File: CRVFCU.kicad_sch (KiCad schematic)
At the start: 150 parts, among them J1 TagConnect_TC2030, J3 USB_C_Receptacle_USB2.0_16P, J4 Micro_SD_Card_Det2, Q3 DMG2301L, Q4 BC818, Q5 DMG2301L, Q6 DMG2301L, SW1 SW_Omron_B3FS, SW2 SW_Nidec_CAS-120A1, U1 MS5611-01BA, U10 W25Q128JVS, U11 CM1624, U12 ESDALC6V1W5, U13 USBLC6-2SC6, U14 USBLC6-2SC6, U15 MAX17049, U16 SI7232DN-T1, U17 SN74LV1T34DCK, U2 STM32H747IITx, U3 LIS2MDL, U4 ICM-45686, U5 FXMA108, U6 AP1117-50, U7 AP1117-33, U8 SI7232DN-T1, U9 USBLC6-4SC6, Y1 32.768khz, Y2 Crystal_GND24, Y3 32.768khz

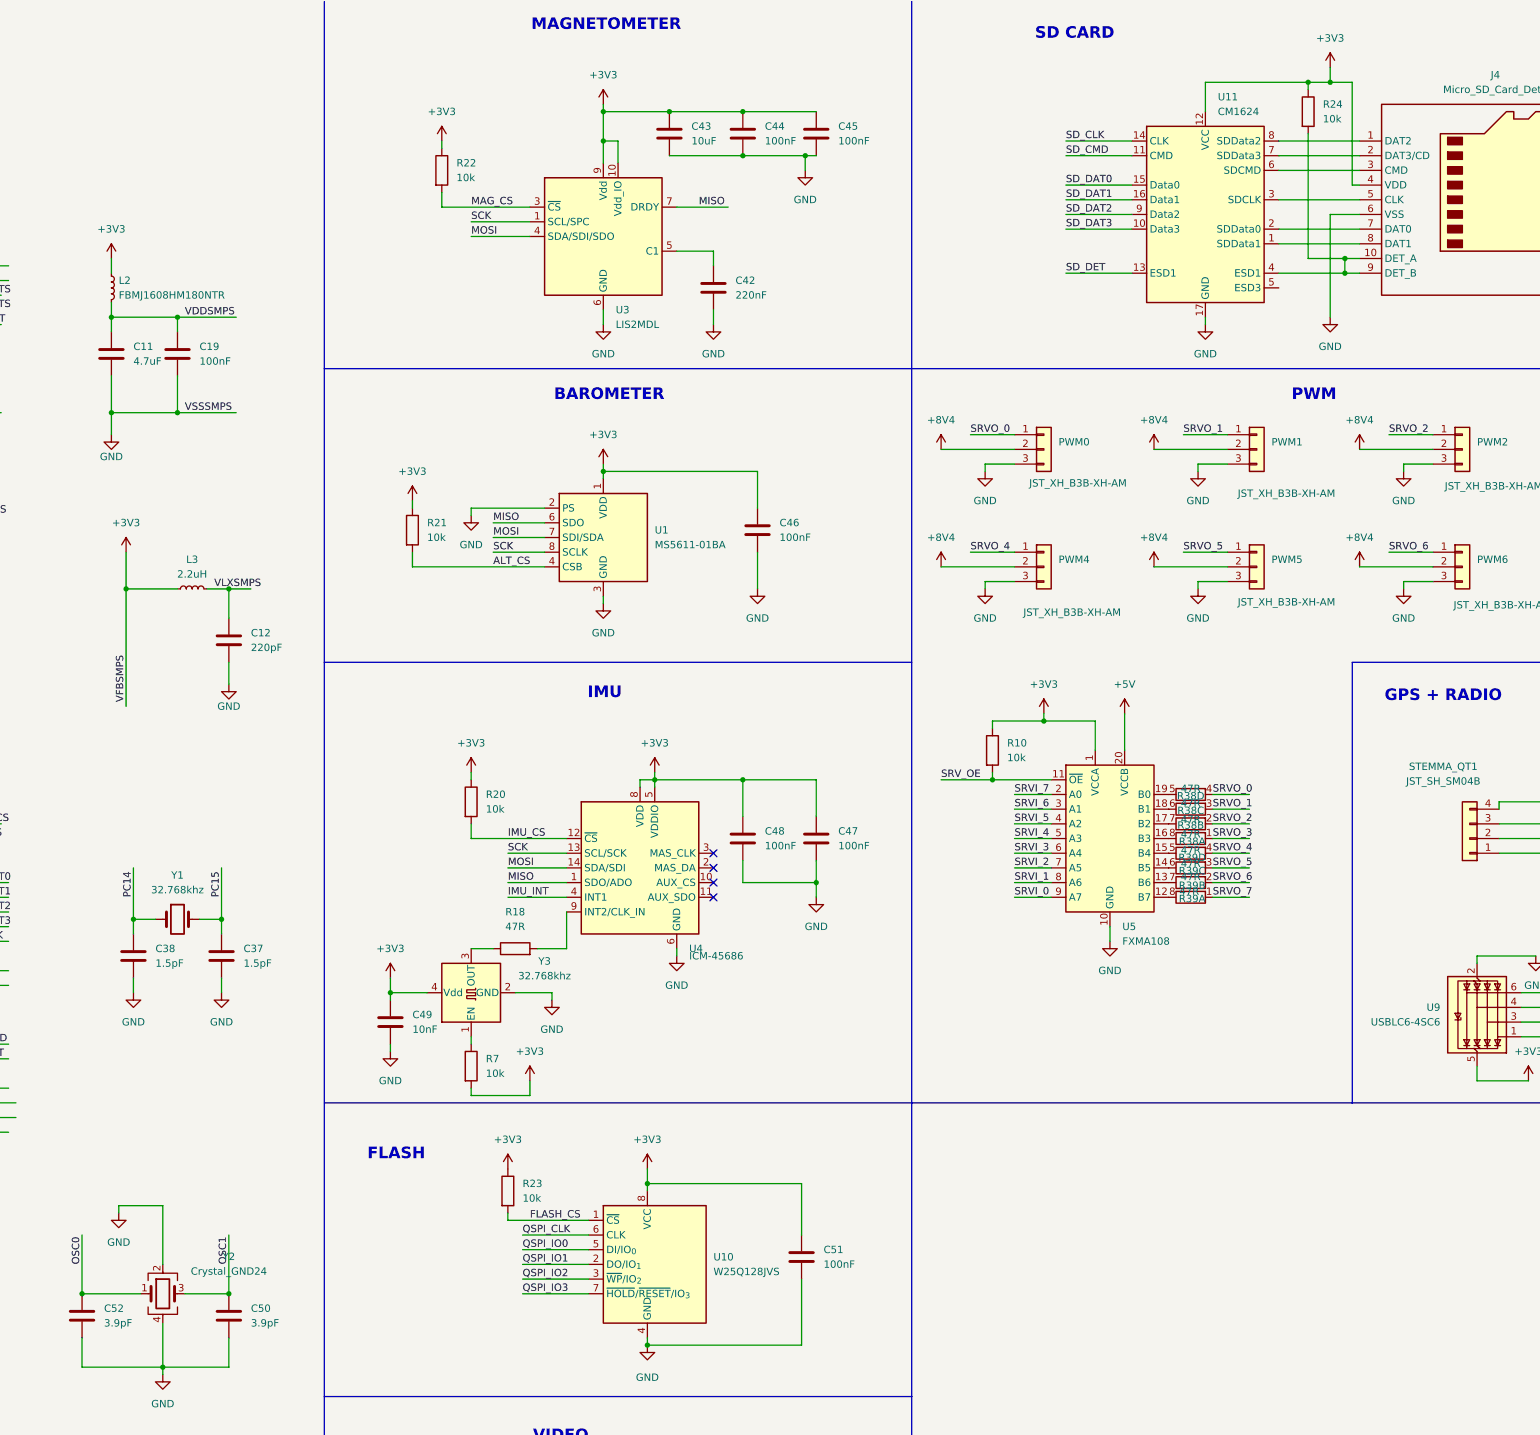
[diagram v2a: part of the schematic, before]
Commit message: rounded corners, added silkscreens, fixed 25mhz oscillator, missing logos but basically finalized
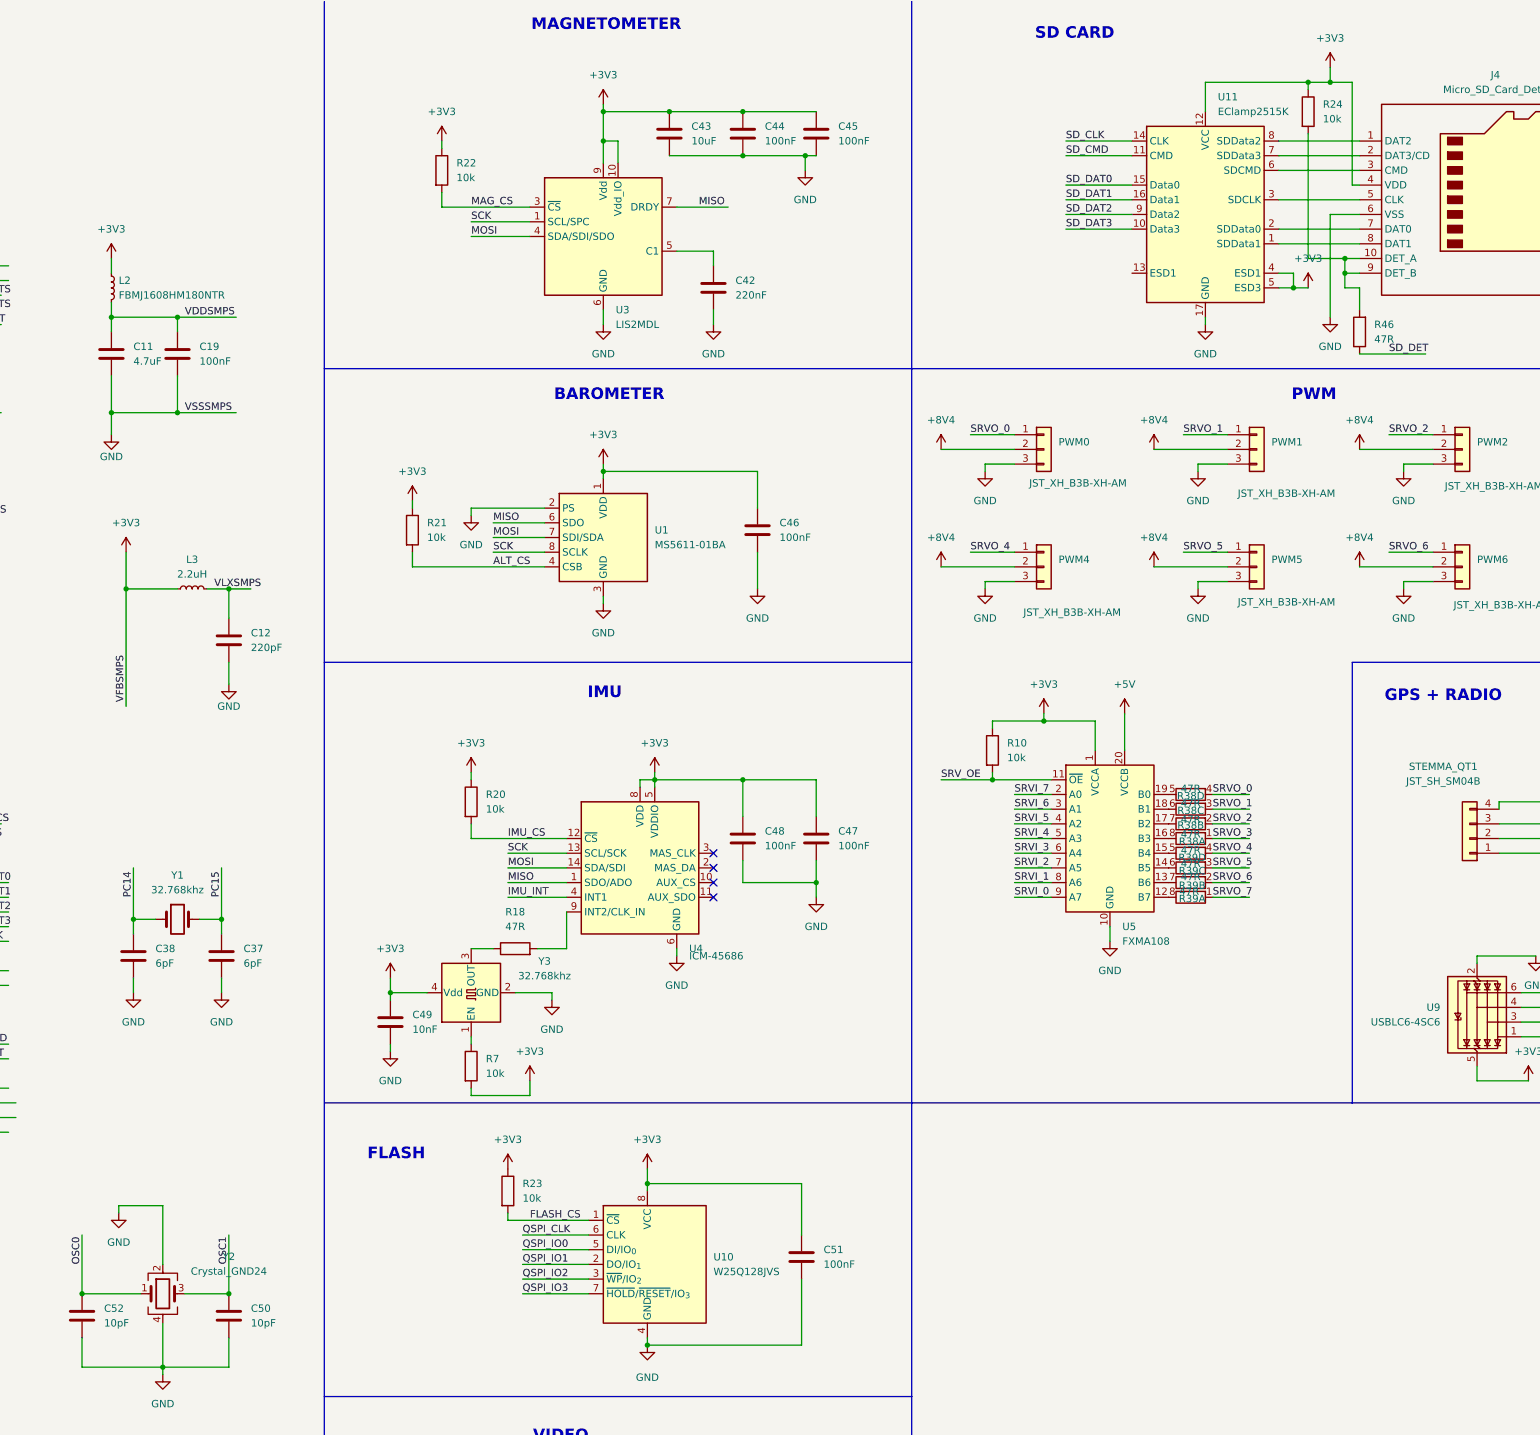
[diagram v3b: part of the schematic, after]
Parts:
- added R46: 47R, Resistor_SMD:R_0402_1005Metric, symbol Device:R
- C37, C38: value 1.5pF -> 6pF
- C50, C52: value 3.9pF -> 10pF
- U11: value CM1624 -> EClamp2515K
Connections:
- net +3V3: now also U11.4 (ESD1), U11.5 (ESD3)
- net SD_DET: now also R46.1; no longer U11.13 (ESD1)
- net at J4.10 (DET_A), J4.9 (DET_B), R24.2: now also R46.2; no longer U11.4 (ESD1)
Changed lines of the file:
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@@
 	)
 	(junction
+		(at 497.84 62.23)
+		(diameter 0)
+		(color 0 0 0 0)
+	)
+	(junction
 		(at 184.15 295.91)
 		(diameter 0)
@@
 	)
 	(junction
-		(at 506.73 59.69)
-		(diameter 0)
-		(color 0 0 0 0)
-	)
-	(junction
 		(at 293.37 67.31)
 		(diameter 0)
@@
 	)
 	(junction
+		(at 506.73 59.69)
+		(diameter 0)
+		(color 0 0 0 0)
+	)
+	(junction
 		(at 162.56 241.3)
 		(diameter 0)
@@
 	(wire
 		(pts
+			(xy 509.27 73.66) (xy 520.7 73.66)
+		)
+		(stroke
+			(width 0)
+			(type default)
+		)
+	)
+	(wire
+		(pts
 			(xy 402.59 161.29) (xy 402.59 165.1)
 		)
@@
 	(wire
 		(pts
+			(xy 509.27 62.23) (xy 506.73 62.23)
+		)
+		(stroke
+			(width 0)
+			(type default)
+		)
+	)
+	(wire
+		(pts
 			(xy 27.94 36.83) (xy 27.94 38.1)
 		)
@@
 	(wire
 		(pts
+			(xy 509.27 66.04) (xy 509.27 62.23)
+		)
+		(stroke
+			(width 0)
+			(type default)
+		)
+	)
+	(wire
+		(pts
 			(xy 415.29 147.32) (xy 415.29 153.67)
 		)
@@
 	(wire
 		(pts
+			(xy 497.84 59.69) (xy 497.84 62.23)
+		)
+		(stroke
+			(width 0)
+			(type default)
+		)
+	)
+	(wire
+		(pts
 			(xy 196.85 275.59) (xy 209.55 275.59)
 		)
@@
 	(wire
 		(pts
-			(xy 495.3 59.69) (xy 506.73 59.69)
+			(xy 497.84 62.23) (xy 500.38 62.23)
 		)
 		(stroke
@@
 	(wire
 		(pts
+			(xy 495.3 62.23) (xy 497.84 62.23)
+		)
+		(stroke
+			(width 0)
+			(type default)
+		)
+	)
+	(wire
+		(pts
 			(xy 402.59 31.75) (xy 415.29 31.75)
 		)
@@
 	(wire
 		(pts
+			(xy 495.3 59.69) (xy 497.84 59.69)
+		)
+		(stroke
+			(width 0)
+			(type default)
+		)
+	)
+	(wire
+		(pts
 			(xy 48.26 125.73) (xy 48.26 127)
 		)
@@
 	(wire
 		(pts
-			(xy 458.47 59.69) (xy 469.9 59.69)
-		)
-		(stroke
-			(width 0)
-			(type default)
-		)
-	)
-	(wire
-		(pts
 			(xy 222.25 284.48) (xy 222.25 285.75)
 		)
@@
 	(wire
 		(pts
+			(xy 506.73 62.23) (xy 506.73 59.69)
+		)
+		(stroke
+			(width 0)
+			(type default)
+		)
+	)
+	(wire
+		(pts
 			(xy 50.8 341.63) (xy 50.8 342.9)
 		)
@@
 		)
 	)
-	(label "SD_DET"
-		(at 458.47 59.69 0)
-		(effects
-			(font
-				(size 1.27 1.27)
-			)
-			(justify left bottom)
-		)
-	)
 	(label "SRVI_3"
 		(at 264.16 160.02 0)
@@
 		)
 	)
+	(label "SD_DET"
+		(at 514.35 73.66 0)
+		(effects
+			(font
+				(size 1.27 1.27)
+			)
+			(justify left bottom)
+		)
+	)
 	(label "PYO1"
 		(at 293.37 330.2 0)
@@
 	)
 	(symbol
+		(lib_id "power:+3V3")
+		(at 500.38 62.23 0)
+		(unit 1)
+		(exclude_from_sim no)
+		(in_bom yes)
+		(on_board yes)
+		(dnp no)
+		(fields_autoplaced yes)
+		(property "Reference" "#PWR0156"
+			(at 500.38 66.04 0)
+			(effects
+				(font
+					(size 1.27 1.27)
+				)
+				(hide yes)
+			)
+		)
+		(property "Value" "+3V3"
+			(at 500.38 57.15 0)
+			(effects
+				(font
+					(size 1.27 1.27)
+				)
+			)
+		)
+		(property "Footprint" ""
+			(at 500.38 62.23 0)
+			(effects
+				(font
+					(size 1.27 1.27)
+				)
+				(hide yes)
+			)
+		)
+		(property "Datasheet" ""
+			(at 500.38 62.23 0)
+			(effects
+				(font
+					(size 1.27 1.27)
+				)
+				(hide yes)
+			)
+		)
+		(property "Description" "Power symbol creates a global label with name \"+3V3\""
+			(at 500.38 62.23 0)
+			(effects
+				(font
+					(size 1.27 1.27)
+				)
+				(hide yes)
+			)
+		)
+		(pin "1"
+		)
+		(instances
+			(project "CRVFCU"
+				(path "/ad8e65f5-b3fb-4c85-9d9e-17b5feb23144"
+					(reference "#PWR0156")
+					(unit 1)
+				)
+			)
+		)
+	)
+	(symbol
 		(lib_id "power:GND")
 		(at 137.16 82.55 0)
@@
 			)
 		)
-		(property "Value" "1.5pF"
+		(property "Value" "6pF"
 			(at 316.23 179.0699 0)
 			(effects
@@
 			)
 		)
-		(property "Value" "CM1624"
+		(property "Value" "EClamp2515K"
 			(at 484.7433 31.75 0)
 			(effects
@@
 			)
 		)
-		(property "Value" "3.9pF"
+		(property "Value" "10pF"
 			(at 317.5 241.2999 0)
 			(effects
@@
 			)
 		)
-		(property "Value" "1.5pF"
+		(property "Value" "6pF"
 			(at 300.99 179.0699 0)
 			(effects
@@
 	)
 	(symbol
+		(lib_id "Device:R")
+		(at 509.27 69.85 180)
+		(unit 1)
+		(exclude_from_sim no)
+		(in_bom yes)
+		(on_board yes)
+		(dnp no)
+		(fields_autoplaced yes)
+		(property "Reference" "R46"
+			(at 511.81 68.5799 0)
+			(effects
+				(font
+					(size 1.27 1.27)
+				)
+				(justify right)
+			)
+		)
+		(property "Value" "47R"
+			(at 511.81 71.1199 0)
+			(effects
+				(font
+					(size 1.27 1.27)
+				)
+				(justify right)
+			)
+		)
+		(property "Footprint" "Resistor_SMD:R_0402_1005Metric"
+			(at 511.048 69.85 90)
+			(effects
+				(font
+					(size 1.27 1.27)
+				)
+				(hide yes)
+			)
+		)
+		(property "Datasheet" "~"
+			(at 509.27 69.85 0)
+			(effects
+				(font
+					(size 1.27 1.27)
+				)
+				(hide yes)
+			)
+		)
+		(property "Description" "Resistor"
+			(at 509.27 69.85 0)
+			(effects
+				(font
+					(size 1.27 1.27)
+				)
+				(hide yes)
+			)
+		)
+		(pin "1"
+		)
+		(pin "2"
+		)
+		(instances
+			(project "CRVFCU"
+				(path "/ad8e65f5-b3fb-4c85-9d9e-17b5feb23144"
+					(reference "R46")
+					(unit 1)
+				)
+			)
+		)
+	)
+	(symbol
 		(lib_id "Device:C")
 		(at 260.35 280.67 0)
@@
 			)
 		)
-		(property "Value" "3.9pF"
+		(property "Value" "10pF"
 			(at 292.1 241.2999 0)
 			(effects

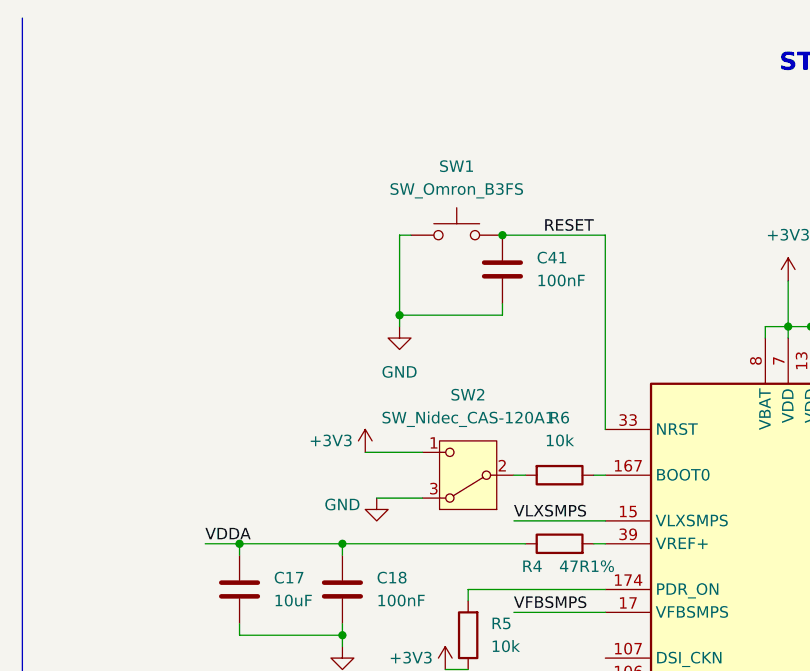
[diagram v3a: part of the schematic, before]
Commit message: changed rst and boot to headers
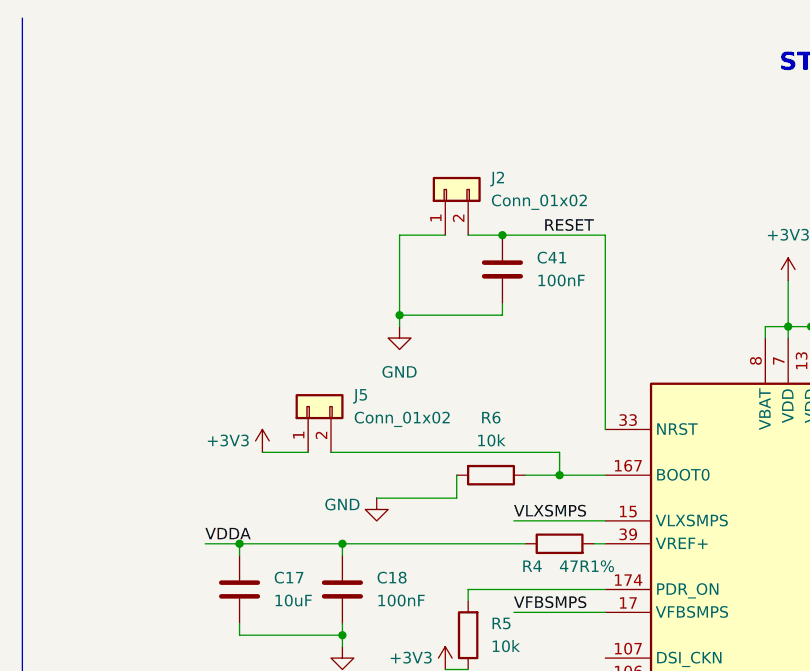
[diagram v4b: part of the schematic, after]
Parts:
- removed SW1: SW_Omron_B3FS, Button_Switch_SMD:SW_SPST_FSMSM, symbol Switch:SW_Omron_B3FS
- removed SW2: SW_Nidec_CAS-120A1, Button_Switch_SMD:Nidec_Copal_CAS-120A, symbol Switch:SW_Nidec_CAS-120A1
- added J2, J5: Conn_01x02, Connector_PinHeader_2.54mm:PinHeader_1x02_P2.54mm_Vertical, symbol Connector_Generic:Conn_01x02
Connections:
- net +3V3: now also J5.1 (Pin_1)
- net GND: now also R6.2, J2.1 (Pin_1)
- net RESET: now also J2.2 (Pin_2)
- net at R6.1, U2.167 (BOOT0): now also J5.2 (Pin_2)
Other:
- moved on the sheet: R6

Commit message: added vref caps and changed some cap values
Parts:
- added C53, C55: 100nF, Capacitor_SMD:C_0402_1005Metric, symbol Device:C
- added C54: 1uF, Capacitor_SMD:C_0402_1005Metric, symbol Device:C
- C17: value 10uF -> 1uF
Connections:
- net +5V: now also C53.1
- net GND: now also J4.10 (DET_A), J4.11 (SHIELD), C53.2, C54.2, C55.2
- net VREF: now reaches R4.2, U2.39 (VREF+)
- net VREF: now also C54.1, C55.1
- net at J4.9 (DET_B), R24.2, R46.2: no longer J4.10 (DET_A)
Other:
- moved on the sheet: C17, C18, R4

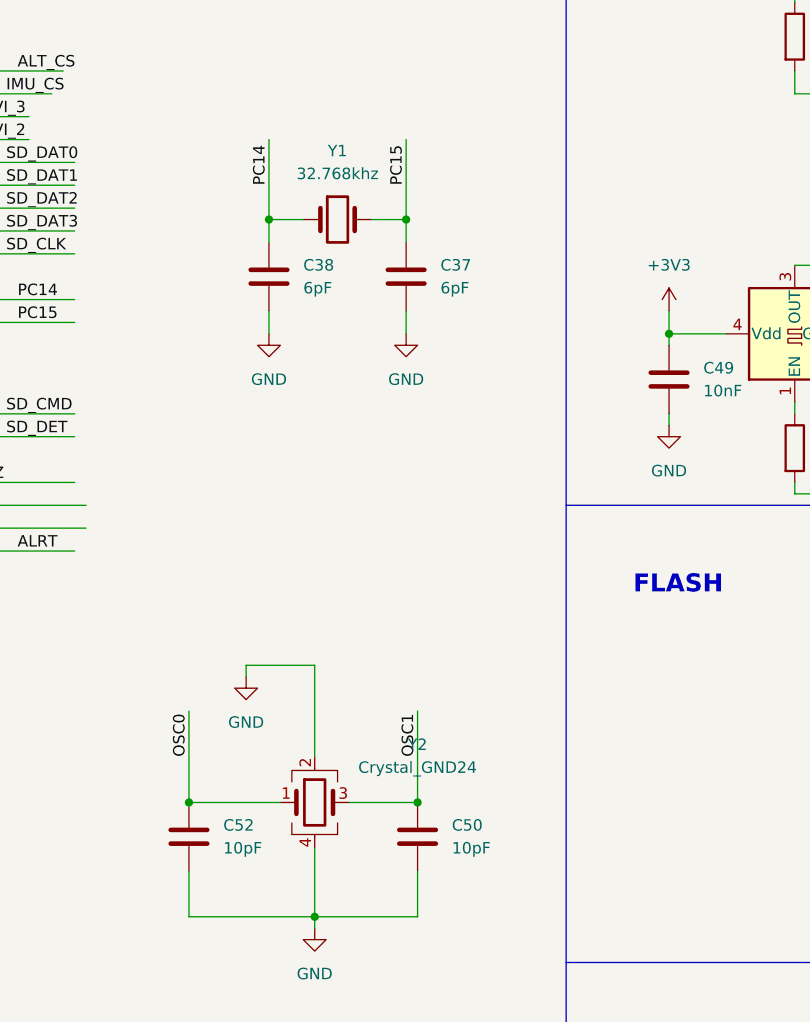
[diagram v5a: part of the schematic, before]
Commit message: adjusted crystals
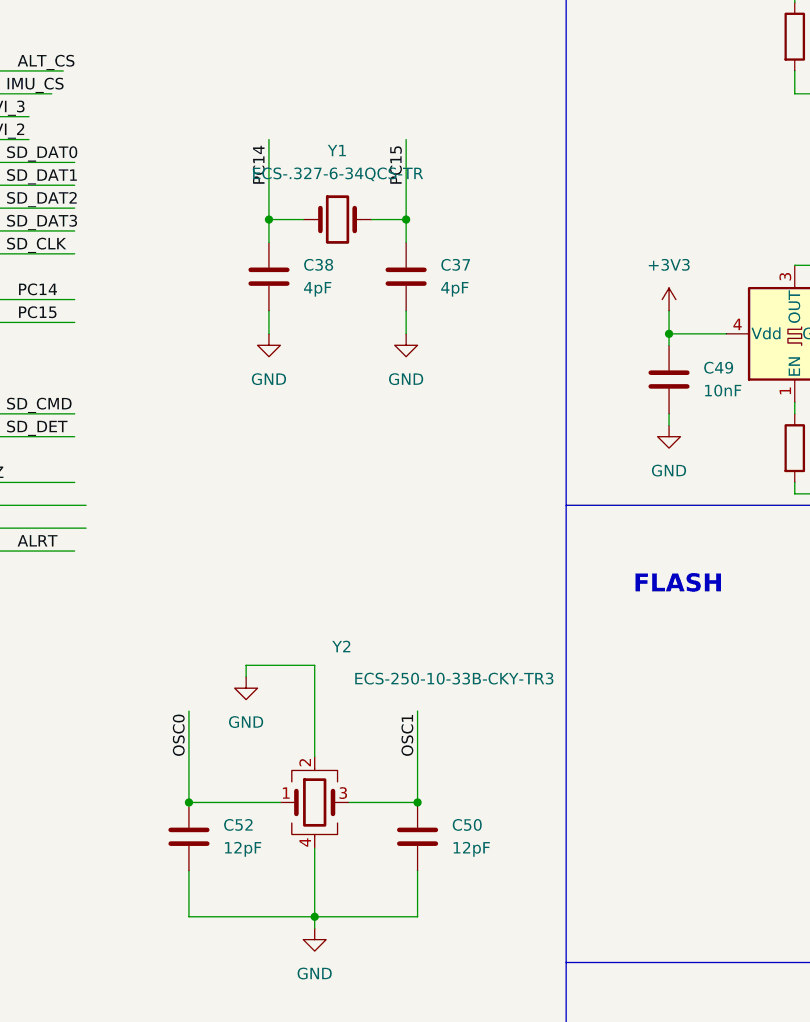
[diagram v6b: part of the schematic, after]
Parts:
- C37, C38: value 6pF -> 4pF
- C50, C52: value 10pF -> 12pF
- Y1: value 32.768khz -> ECS-.327-6-34QCS-TR
- Y2: value Crystal_GND24 -> ECS-250-10-33B-CKY-TR3
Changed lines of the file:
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@@
 			)
 		)
-		(property "Value" "32.768khz"
+		(property "Value" "ECS-.327-6-34QCS-TR"
 			(at 304.8 166.37 0)
 			(effects
@@
 			)
 		)
-		(property "Value" "6pF"
+		(property "Value" "4pF"
 			(at 316.23 179.0699 0)
 			(effects
@@
 			)
 		)
-		(property "Value" "10pF"
+		(property "Value" "12pF"
 			(at 317.5 241.2999 0)
 			(effects
@@
 			)
 		)
-		(property "Value" "6pF"
+		(property "Value" "4pF"
 			(at 300.99 179.0699 0)
 			(effects
@@
 			)
 		)
-		(property "Value" "10pF"
+		(property "Value" "12pF"
 			(at 292.1 241.2999 0)
 			(effects
@@
 		(on_board yes)
 		(dnp no)
-		(fields_autoplaced yes)
 		(property "Reference" "Y2"
-			(at 313.69 229.7998 0)
+			(at 305.308 218.948 0)
 			(effects
 				(font
@@
 			)
 		)
-		(property "Value" "Crystal_GND24"
-			(at 313.69 232.3398 0)
+		(property "Value" "ECS-250-10-33B-CKY-TR3"
+			(at 317.754 222.504 0)
 			(effects
 				(font
